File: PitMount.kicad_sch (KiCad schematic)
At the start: 15 parts, among them J1 Conn_01x08_Pin, Q1 BC817, Q2 IRLML6401, U1 UnifyNano, U2 ELRS-Rx

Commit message: Add title block to schematic and PCB sheets
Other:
- company: (none) -> Bentprop Electronics
- title: (none) -> PitMount
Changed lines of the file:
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@@
 (kicad_sch (version 20221206) (generator eeschema)
   (paper "A4")
+  (title_block
+    (title "PitMount")
+    (date "2023-01-19")
+    (rev "0.1.0")
+    (company "Bentprop Electronics")
+    (comment 1 "© 2023 Nils Hofmann")
+  )
   (junction (at 250.825 24.765) (diameter 0) (color 0 0 0 0)
   )

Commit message: Exclude non-populatable symbols from BOM
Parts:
- H1, H2, H3, H4, J1, JP1: now left out of the parts list
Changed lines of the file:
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@@
   )
   (symbol (lib_id "Connector:Conn_01x08_Pin") (at 43.434 37.084 0) (unit 1)
-    (in_bom yes) (on_board yes) (dnp no)
+    (in_bom no) (on_board yes) (dnp no)
     (property "Reference" "J1" (at 44.069 23.749 0)
       (effects (font (size 1.27 1.27)))
@@
   )
   (symbol (lib_id "Mechanical:MountingHole_Pad") (at 258.445 24.765 270) (unit 1)
-    (in_bom yes) (on_board yes) (dnp no) (fields_autoplaced)
+    (in_bom no) (on_board yes) (dnp no) (fields_autoplaced)
     (property "Reference" "H2" (at 262.255 23.4949 90)
       (effects (font (size 1.27 1.27)) (justify left))
@@
   )
   (symbol (lib_id "Mechanical:MountingHole_Pad") (at 258.445 20.32 270) (unit 1)
-    (in_bom yes) (on_board yes) (dnp no) (fields_autoplaced)
+    (in_bom no) (on_board yes) (dnp no) (fields_autoplaced)
     (property "Reference" "H1" (at 262.255 19.0499 90)
       (effects (font (size 1.27 1.27)) (justify left))
@@
   )
   (symbol (lib_id "Jumper:SolderJumper_2_Open") (at 96.52 102.87 0) (unit 1)
-    (in_bom yes) (on_board yes) (dnp no) (fields_autoplaced)
+    (in_bom no) (on_board yes) (dnp no) (fields_autoplaced)
     (property "Reference" "JP1" (at 96.52 97.79 0)
       (effects (font (size 1.27 1.27)))
@@
   )
   (symbol (lib_id "Mechanical:MountingHole_Pad") (at 258.445 29.21 270) (unit 1)
-    (in_bom yes) (on_board yes) (dnp no) (fields_autoplaced)
+    (in_bom no) (on_board yes) (dnp no) (fields_autoplaced)
     (property "Reference" "H3" (at 262.255 27.9399 90)
       (effects (font (size 1.27 1.27)) (justify left))
@@
   )
   (symbol (lib_id "Mechanical:MountingHole_Pad") (at 258.445 33.655 270) (unit 1)
-    (in_bom yes) (on_board yes) (dnp no) (fields_autoplaced)
+    (in_bom no) (on_board yes) (dnp no) (fields_autoplaced)
     (property "Reference" "H4" (at 262.255 32.3849 90)
       (effects (font (size 1.27 1.27)) (justify left))

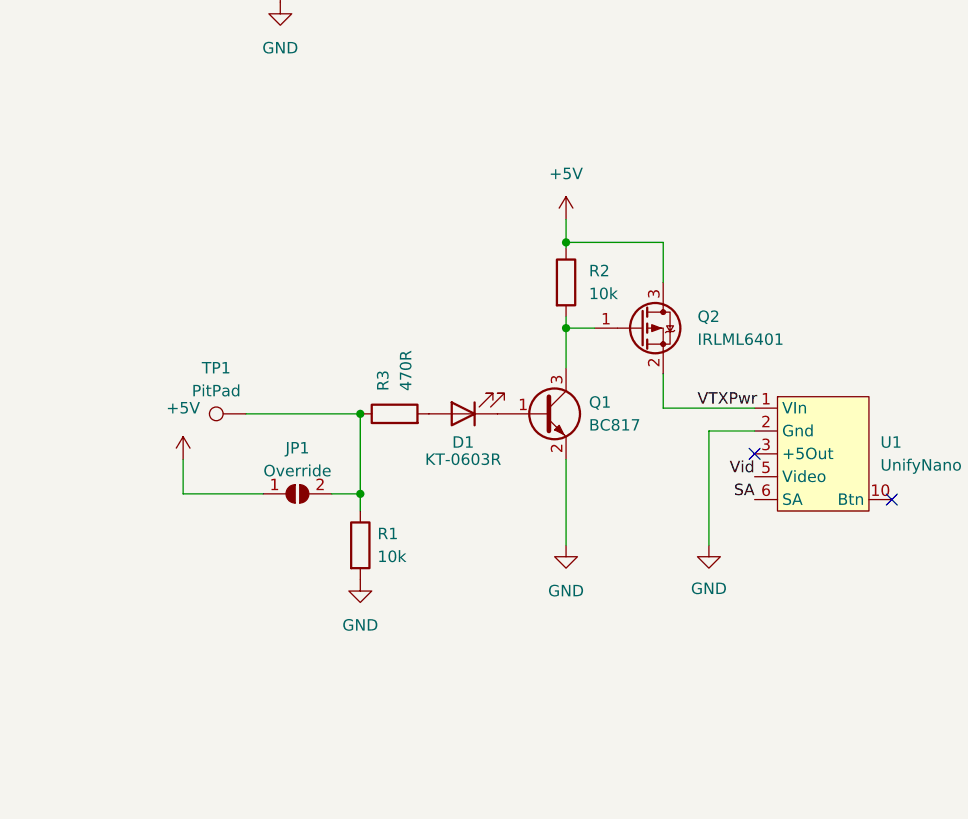
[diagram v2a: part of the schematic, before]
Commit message: Switch to an n-channel FET
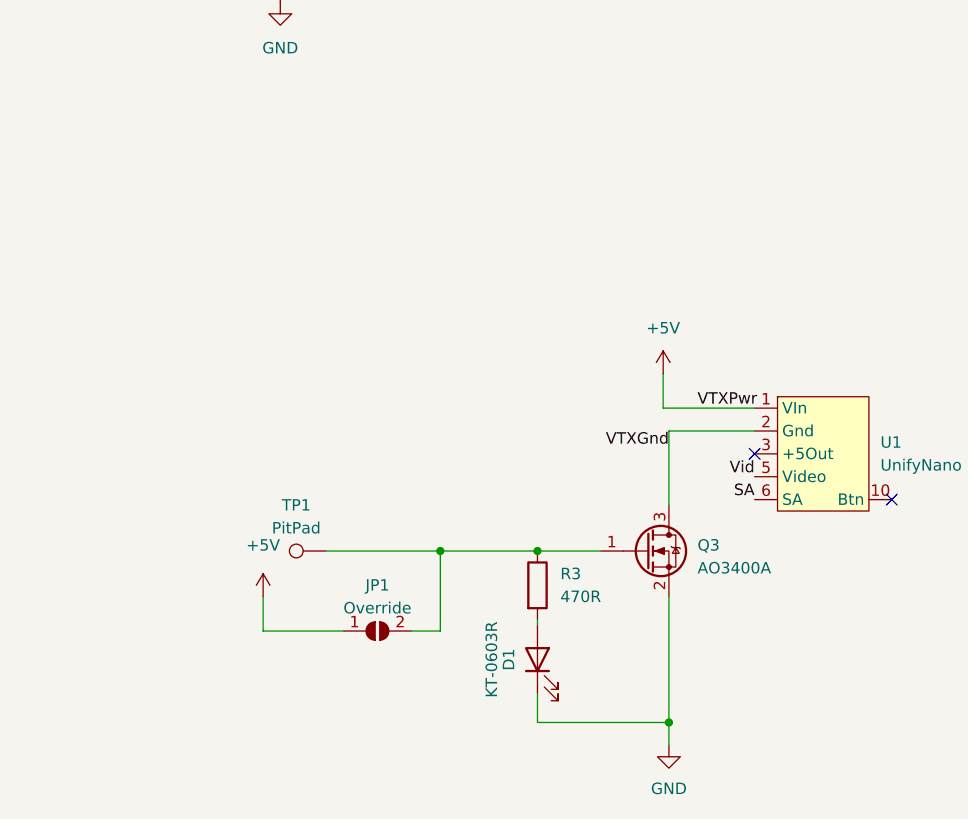
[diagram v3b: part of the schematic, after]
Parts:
- removed Q1: BC817, Package_TO_SOT_SMD:SOT-23, symbol Transistor_BJT:BC817
- removed Q2: IRLML6401, Package_TO_SOT_SMD:SOT-23, symbol Transistor_FET:IRLML6401
- removed R1, R2: 10k, Resistor_SMD:R_0402_1005Metric, symbol Device:R
- added Q3: AO3400A, Package_TO_SOT_SMD:SOT-23, symbol Transistor_FET:AO3400A
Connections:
- net VTXPwr is gone; now on net +5V: U1.1 (VIn)
- net GND: now also D1.1 (K), Q3.2 (S); no longer U1.2 (Gnd), U1.4 (Gnd), U1.7 (Gnd), U1.8 (Gnd), U1.9 (Gnd)
- net at JP1.2 (B), R3.1, TP1.1: now also Q3.1 (G)
- new net VTXGnd: Q3.3 (D), U1.2 (Gnd), U1.4 (Gnd), U1.7 (Gnd), U1.8 (Gnd), U1.9 (Gnd)
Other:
- moved on the sheet: D1, JP1, R3, TP1
